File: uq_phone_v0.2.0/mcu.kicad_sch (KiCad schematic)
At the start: 34 parts, among them J6 Conn_ARM_SWD_TagConnect_TC2030, J7 559092474, J9 559092474, Q1 MMBT3904LP-7, Q2 MMBT3904LP-7, U16 TXB0108YZPR2, U5 TCA9509MRVHR, U6 STM32H733VGHx, U7 TXB0108YZPR2

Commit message: More routing and moving cellular to new project
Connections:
- net DISP_BL: now also U6.J3 (PA6); no longer U6.J7 (PB10)
- net PB_0: no longer U6.C4 (PE1)
- net PB_1: now also U6.C3 (PE4); no longer U6.B3 (PE3)
- net PB_2: no longer U6.C3 (PE4)
- net PB_3: no longer U6.D3 (PE5)
- net PB_4: now also U6.C1 (PH0); no longer U6.E3 (PE6)
- net PB_5: no longer U6.K7 (PB11)
- net PB_6: no longer U6.K8 (PB12)
- net PB_7: now also U6.D3 (PE5); no longer U6.B1 (PC15)
- net PB_8: no longer U6.C1 (PH0)
- net PB_9: no longer U6.D1 (PH1)
- net PB_CALL: now also U6.B1 (PC15); no longer U6.C6 (PD6)
- net PB_DPAD_DOWN: now also U6.B3 (PE3); no longer U6.A6 (PB4(NJTRST))
- net PB_DPAD_LEFT: now also U6.G4 (PC4); no longer U6.B5 (PB6)
- net PB_DPAD_RIGHT: no longer U6.C5 (PB5)
- net PB_DPAD_SELECT: now also U6.F1 (PC0); no longer U6.A5 (PB7)
- net PB_DPAD_UP: now also U6.F2 (PC1); no longer U6.B6 (PD5)
- net PB_END_CALL: no longer U6.A8 (PA15(JTDI))
- net PB_HASH: no longer U6.A3 (PE2)
- net PB_MENU_L: now also U6.G2 (PA0); no longer U6.F1 (PC0)
- net PB_MENU_R: no longer U6.F2 (PC1)
- net PB_PWR: no longer U6.G2 (PA0)
- net PB_STAR: now also U6.E3 (PE6); no longer U6.D4 (PE0)
- net VIB_EN: now also U6.K5 (PE9); no longer U6.G4 (PC4)
- net VIB_PWM: now also U6.K4 (PB1); no longer U6.J3 (PA6)
- net DISP_SDA: now reaches U6.G7 (PE14)
- net DISP_RESET: now reaches U6.G8 (PD15)
- net DISP_DC: now reaches U6.H8 (PD14)
- net DISP_SCL: now reaches U6.J6 (PE12)
- net DISP_CS: now reaches U6.J8 (PB13)

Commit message: Most routing complete
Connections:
- net PB_0: now also U6.A3 (PE2)
- net PB_2: now also U6.A5 (PB7)
- net PB_3: now also U6.A6 (PB4(NJTRST))
- net PB_5: now also U6.C5 (PB5)
- net PB_6: now also U6.B6 (PD5)
- net PB_8: now also U6.C4 (PE1)
- net PB_9: now also U6.B5 (PB6)
- net PB_DPAD_RIGHT: now also U6.C6 (PD6)
- net PB_END_CALL: now also U6.D6 (PD7)
- net PB_HASH: now also U6.D4 (PE0)
- net PB_MENU_R: now also U6.D7 (PD4)
- net PB_PWR: now also U6.K8 (PB12)

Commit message: More roting and vias
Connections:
- net GND: now also J9.5, J9.6, J9.7, J9.8
- no-connect marks 4 -> 18

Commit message: DRC and routing fixing
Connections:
- net POWER_SW: now reaches U6.E8 (PD1)
- no-connect marks 18 -> 17

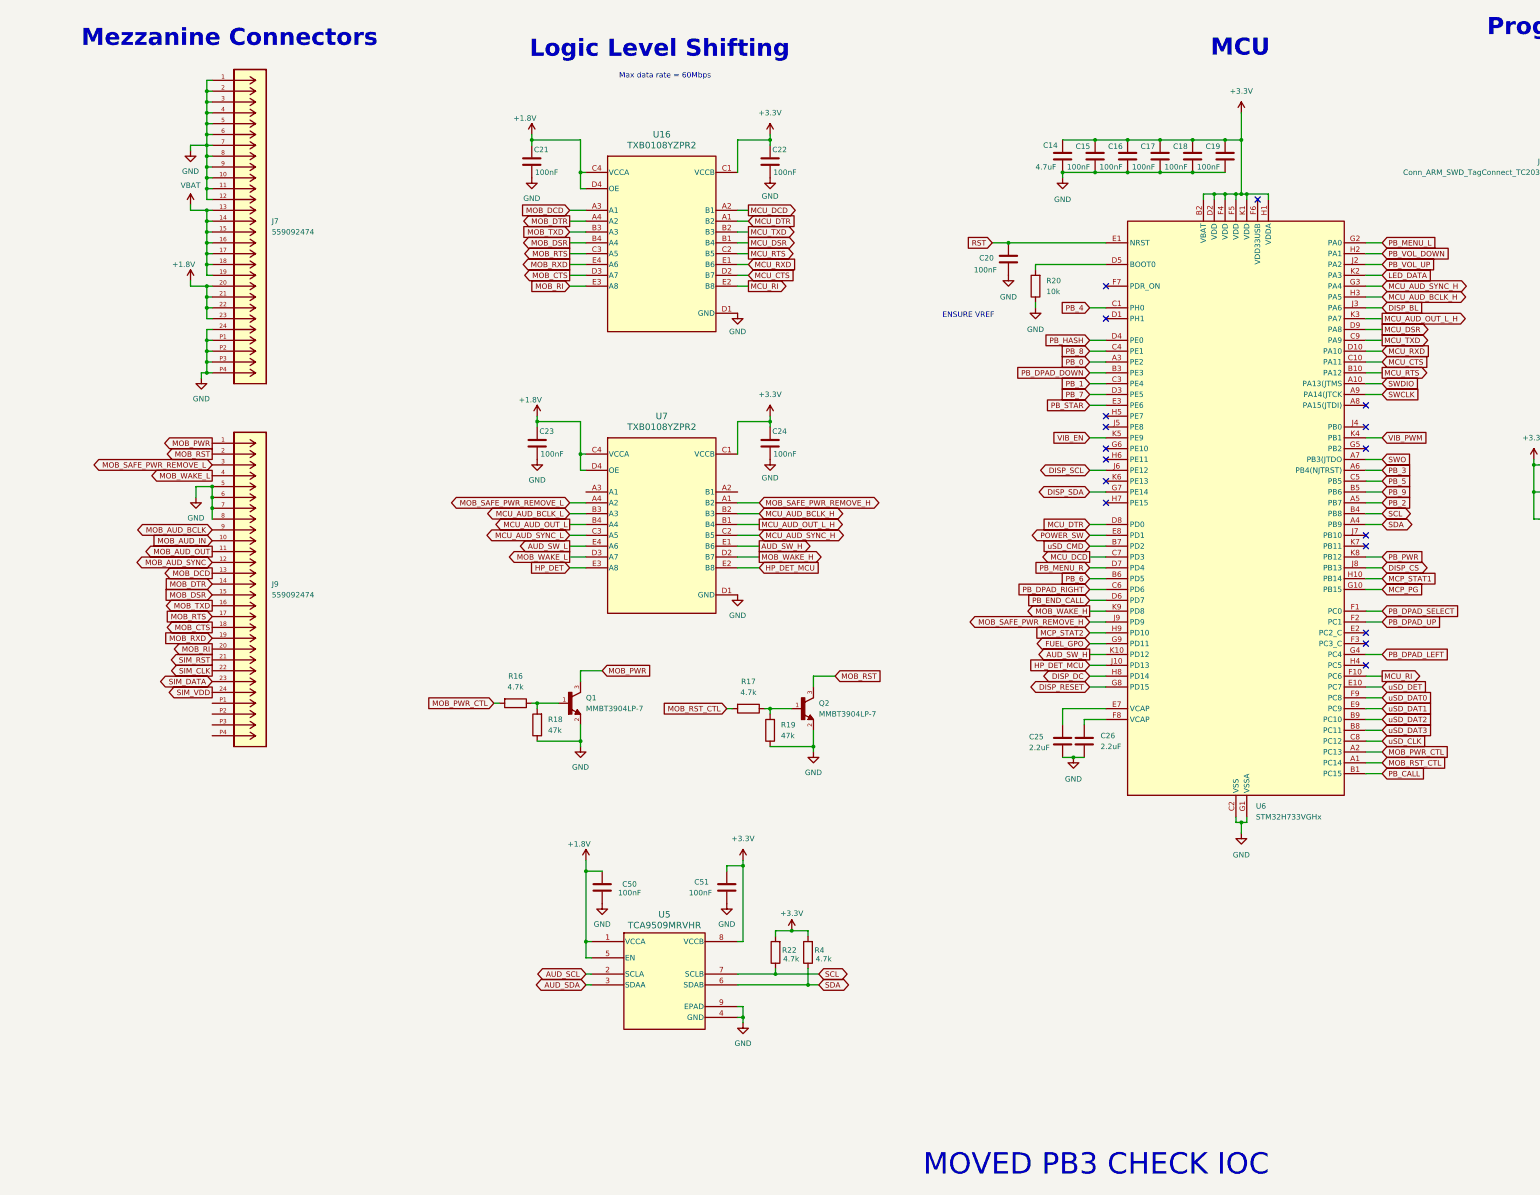
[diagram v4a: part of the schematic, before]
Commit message: New logic level shifters
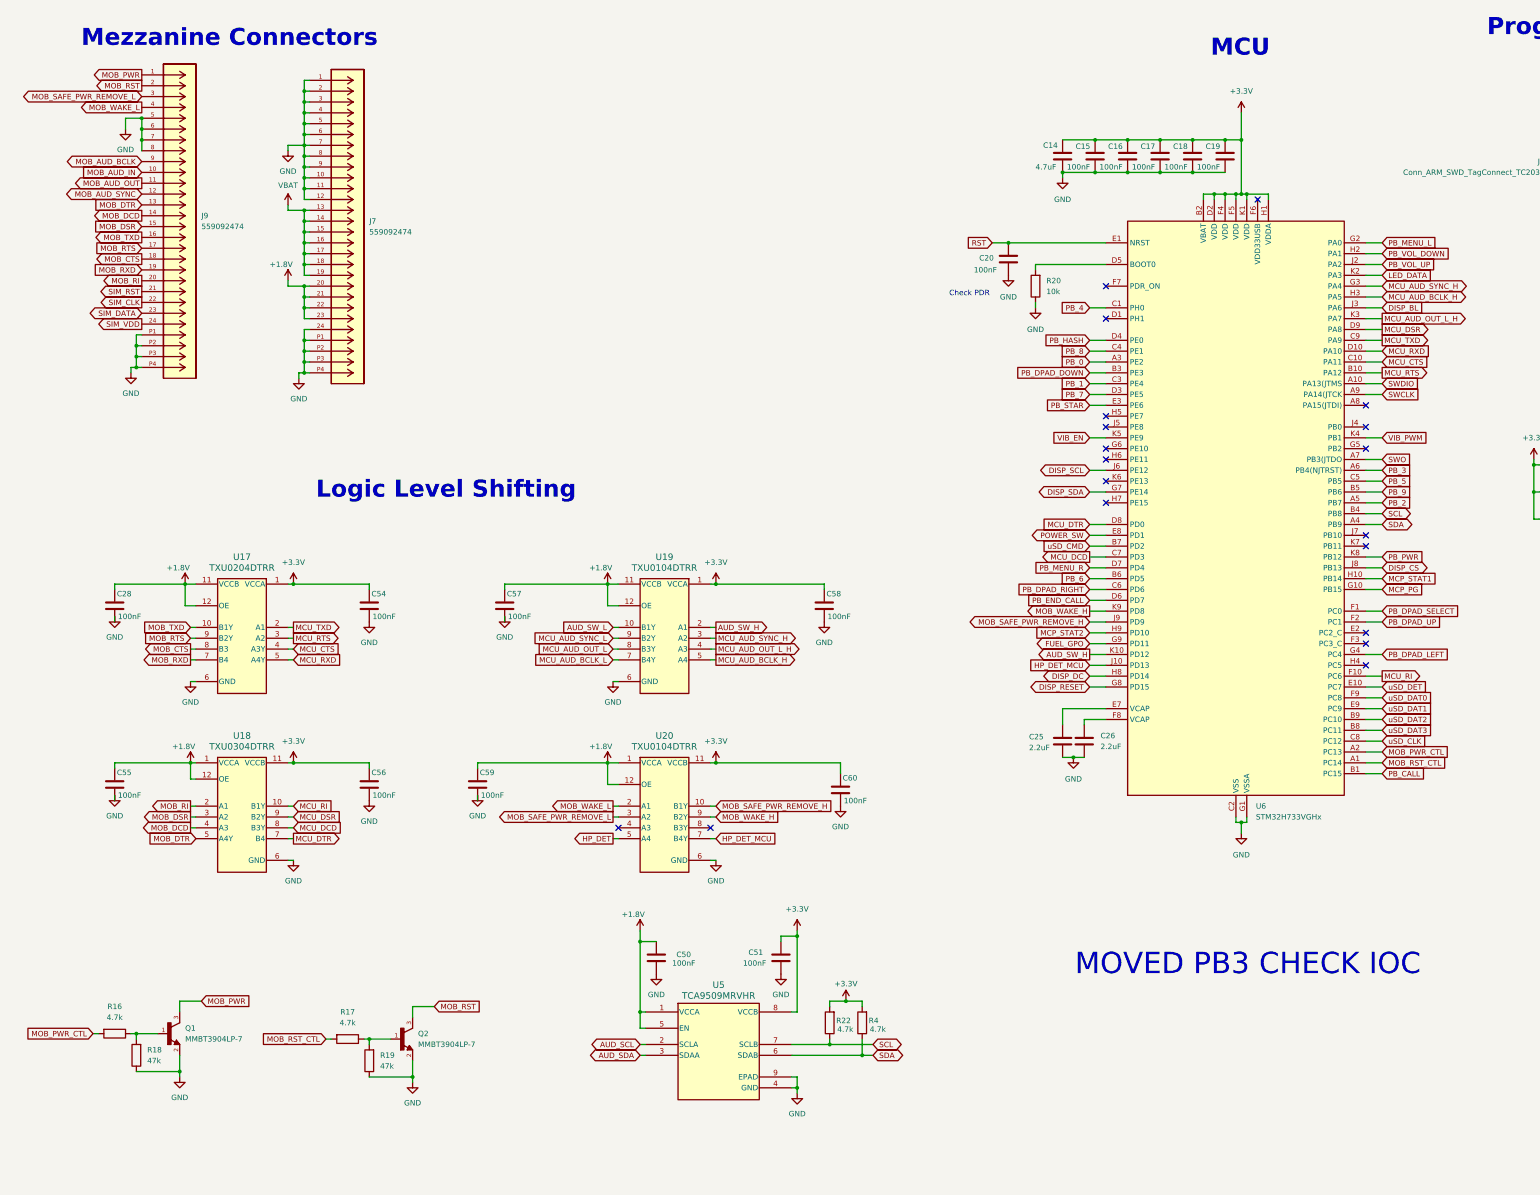
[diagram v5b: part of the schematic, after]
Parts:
- removed C21, C22, C23, C24: 100nF, Capacitor_SMD:C_0201_0603Metric, symbol Capacitors:capacitor_100nF
- removed U16, U7: TXB0108YZPR2, TXB0108YZPR2:YZP20, symbol TXB0108YZPR2:TXB0108YZPR2
- added C28, C54, C55, C56, C57, C58, C59, C60: 100nF, Capacitor_SMD:C_0201_0603Metric, symbol Capacitors:capacitor_100nF
- added U17: TXU0204DTRR, TXU0x04DTRR:DTR0012A-MFG, symbol TXU0204:TXU0204DTRR
- added U18: TXU0304DTRR, TXU0x04DTRR:DTR0012A-MFG, symbol TXU0304:TXU0304DTRR
- added U19, U20: TXU0104DTRR, TXU0x04DTRR:DTR0012A-MFG, symbol TXU0104:TXU0104DTRR
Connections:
- net +1.8V: now also C28.1, C55.1, C57.1, C59.1, U17.11 (VCCB), U17.12 (OE), U18.1 (VCCA), U18.12 (OE), U19.11 (VCCB), U19.12 (OE), U20.1 (VCCA), U20.12 (OE)
- net +3.3V: now also C54.1, C56.1, C58.1, C60.1, U17.1 (VCCA), U18.11 (VCCB), U19.1 (VCCA), U20.11 (VCCB)
- net AUD_SW_H: now also U19.2 (A1)
- net AUD_SW_L: now also U19.10 (B1Y)
- net GND: now also J9.P1, J9.P2, J9.P3, J9.P4, C28.2, C54.2, C55.2, C56.2, C57.2, C58.2, C59.2, C60.2, U17.6 (GND), U18.6 (GND), U19.6 (GND), U20.6 (GND)
- net HP_DET: now also U20.5 (A4)
- net HP_DET_MCU: now also U20.7 (B4Y)
- net MCU_AUD_BCLK_H: now also U19.5 (A4)
- net MCU_AUD_BCLK_L: now also U19.7 (B4Y)
- net MCU_AUD_OUT_L: now also U19.8 (B3Y)
- net MCU_AUD_OUT_L_H: now also U19.4 (A3)
- net MCU_AUD_SYNC_H: now also U19.3 (A2)
- net MCU_AUD_SYNC_L: now also U19.9 (B2Y)
- net MCU_CTS: now also U17.4 (A3Y)
- net MCU_DCD: now also U18.8 (B3Y)
- net MCU_DSR: now also U18.9 (B2Y)
- net MCU_DTR: now also U18.7 (B4)
- net MCU_RI: now also U18.10 (B1Y)
- net MCU_RTS: now also U17.3 (A2)
- net MCU_RXD: now also U17.5 (A4Y)
- net MCU_TXD: now also U17.2 (A1)
- net MOB_CTS: now also U17.8 (B3)
- net MOB_DCD: now also J9.14, U18.4 (A3); no longer J9.13
- net MOB_DSR: now also U18.3 (A2)
- net MOB_DTR: now also J9.13, U18.5 (A4Y); no longer J9.14
- net MOB_RI: now also U18.2 (A1)
- net MOB_RTS: now also U17.9 (B2Y)
- net MOB_RXD: now also U17.7 (B4)
- net MOB_SAFE_PWR_REMOVE_H: now also U20.10 (B1Y)
- net MOB_SAFE_PWR_REMOVE_L: now also U20.3 (A2)
- net MOB_TXD: now also U17.10 (B1Y)
- net MOB_WAKE_H: now also U20.9 (B2Y)
- net MOB_WAKE_L: now also U20.2 (A1)
- no-connect marks 17 -> 19
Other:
- note added: "Check PDR"
- note removed: "ENSURE VREF"
- note removed: "Max data rate = 60Mbps"
- moved on the sheet: C50, C51, J7, J9, Q1, Q2, R16, R17, R18, R19, R22, R4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
